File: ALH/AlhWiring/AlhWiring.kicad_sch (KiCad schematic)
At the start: 18 parts, among them J317 Relay_109, SW1 SW_Push_Open, SW2 SW_Push, T10e_car Conn_01x10_Socket, T10e_engine Black Connector, T10h_car Conn_01x10_Socket, T10h_engine Blue Connector, T10w_car Conn_01x10_Socket, T10w_engine White Connector, T14a_car 14pin Connector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

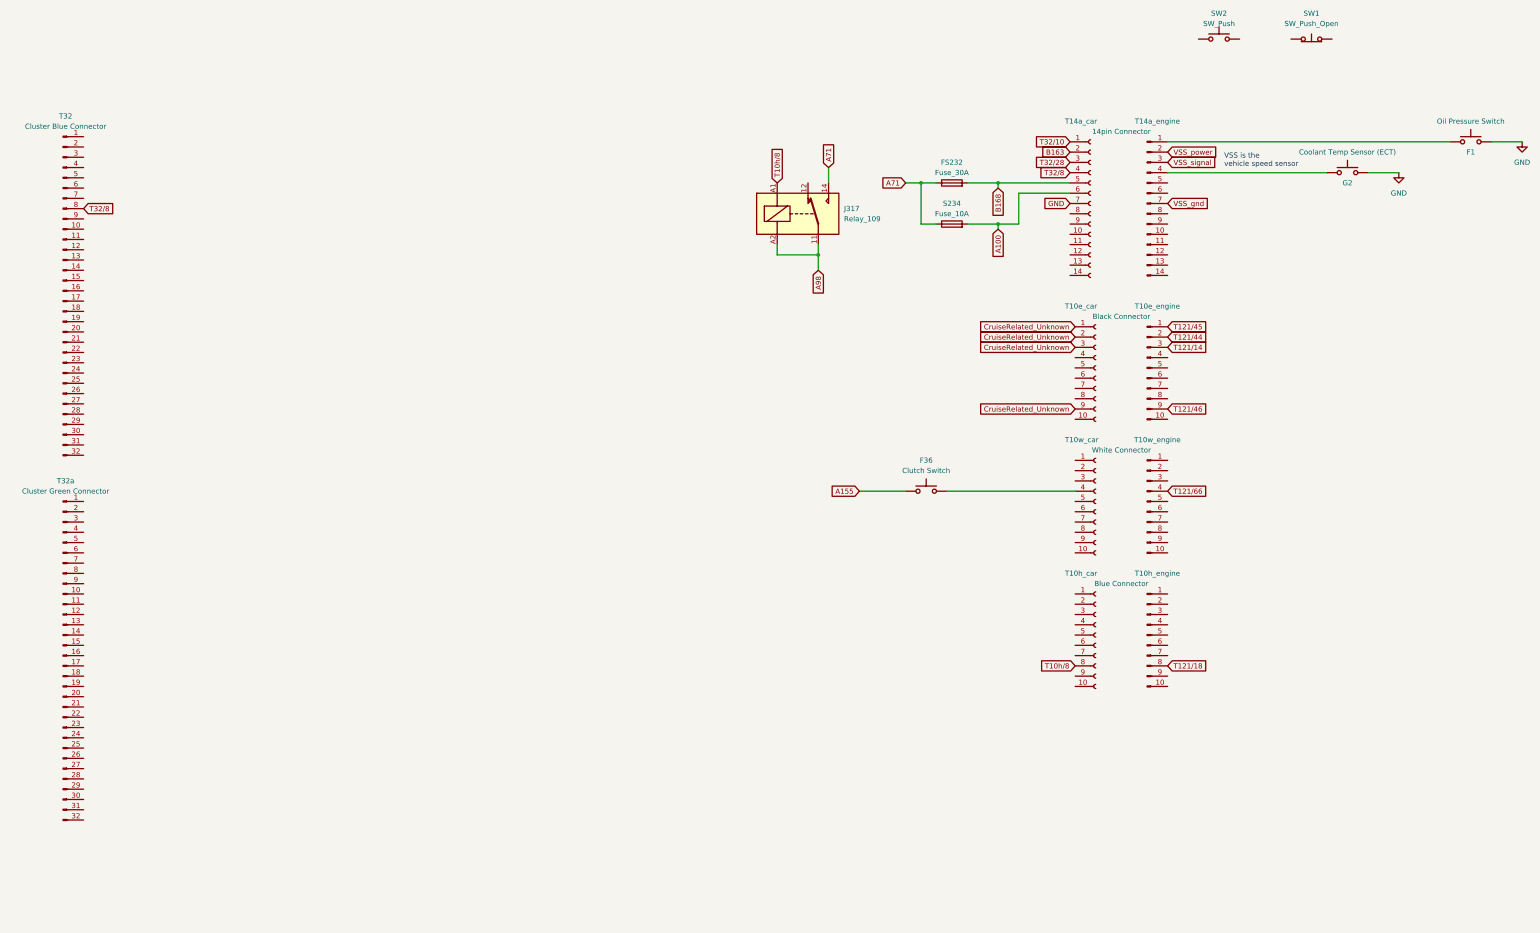
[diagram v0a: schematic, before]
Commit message: Finish ALH diagram.  Few parts still need to be reviewed.
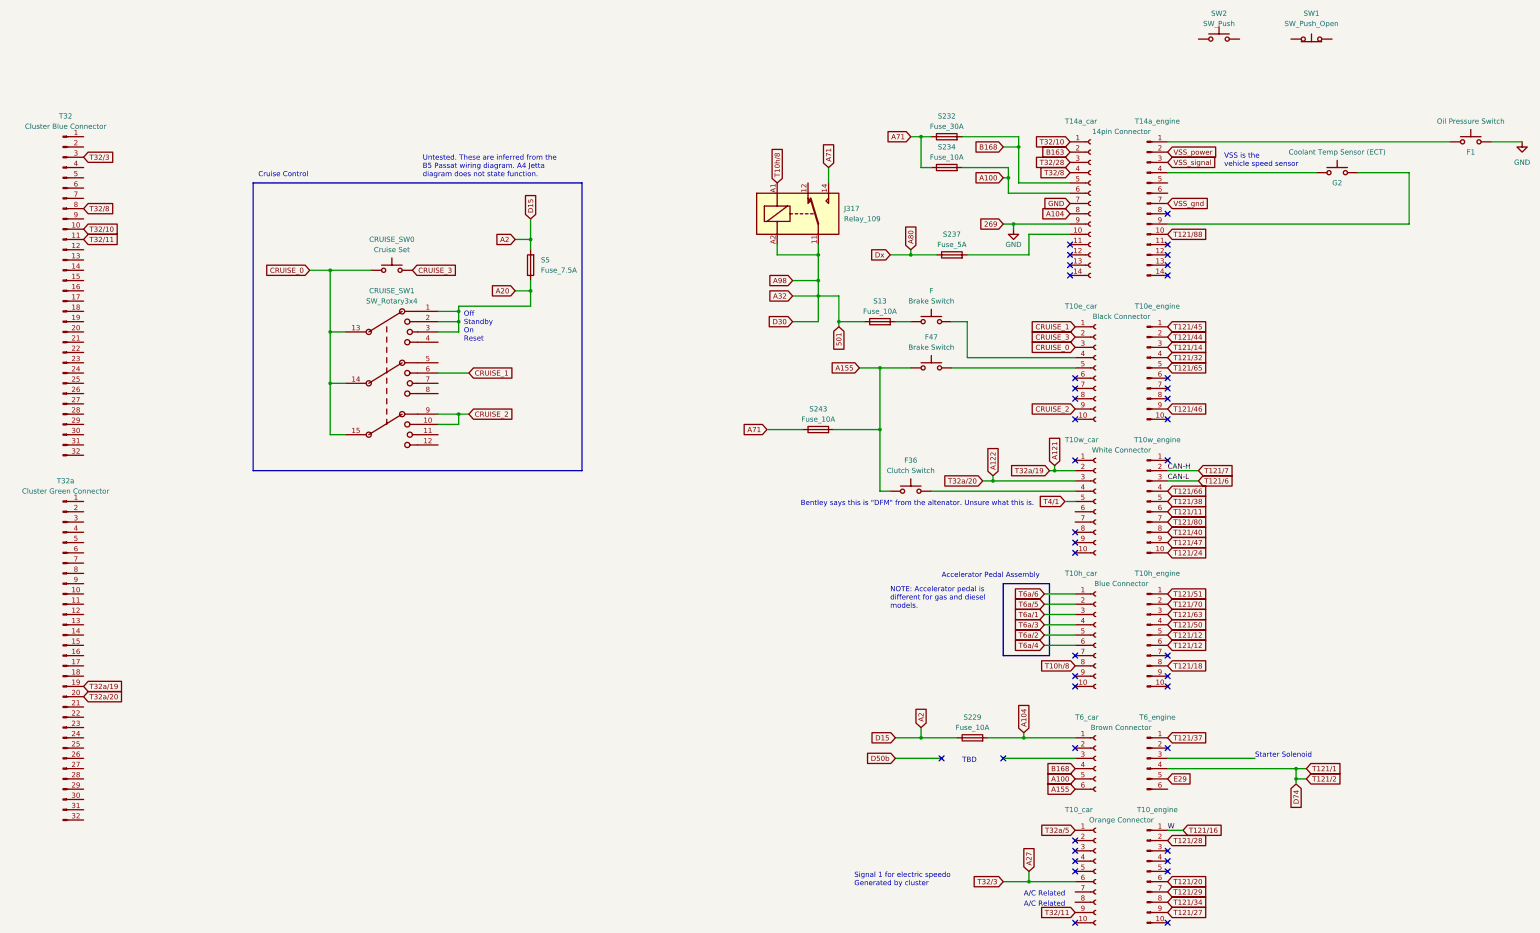
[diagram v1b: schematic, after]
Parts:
- added CRUISE_SW0: Cruise Set, symbol Switch:SW_Push
- added CRUISE_SW1: SW_Rotary3x4, symbol Switch:SW_Rotary3x4
- added F, F47: Brake Switch, symbol Switch:SW_Push
- added S13, S229, S243: Fuse_10A, symbol Device:Fuse
- added S237: Fuse_5A, symbol Device:Fuse
- added S5: Fuse_7.5A, symbol Device:Fuse
- added T10_car: Conn_01x10_Socket, symbol Connector:Conn_01x10_Socket
- added T10_engine: Orange Connector, symbol Connector:Conn_01x10_Pin
- added T6_car: Brown Connector, symbol Connector:Conn_01x06_Socket
- added T6_engine: Conn_01x06_Pin, symbol Connector:Conn_01x06_Pin
- renumbered FS232 to S232
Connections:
- net A100: now also T6_car.5 (Pin_5)
- net A155: now also F47.1, S243.2, T6_car.6 (Pin_6)
- net A71: now also S243.1
- net B168: now also T6_car.4 (Pin_4)
- net GND: now also T14a_car.9 (Pin_9); no longer G2.2
- net T32/10: now also T32.10 (Pin_10)
- net T32/11: now reaches T32.11 (Pin_11)
- net T32/11: now also T10_car.9 (Pin_9)
- net A27: now reaches T32.3 (Pin_3)
- net A27: now also T10_car.6 (Pin_6)
- net T121/24: now reaches T10w_engine.10 (Pin_10)
- net T121/7: now reaches T10w_engine.2 (Pin_2)
- net T121/6: now reaches T10w_engine.3 (Pin_3)
- net T121/38: now reaches T10w_engine.5 (Pin_5)
- net T121/11: now reaches T10w_engine.6 (Pin_6)
- net T121/80: now reaches T10w_engine.7 (Pin_7)
- net T121/40: now reaches T10w_engine.8 (Pin_8)
- net T121/47: now reaches T10w_engine.9 (Pin_9)
- net T121/32: now reaches T10e_engine.4 (Pin_4)
- net T121/65: now reaches T10e_engine.5 (Pin_5)
- net T121/51: now reaches T10h_engine.1 (Pin_1)
- net T121/70: now reaches T10h_engine.2 (Pin_2)
- net T121/63: now reaches T10h_engine.3 (Pin_3)
- net T121/50: now reaches T10h_engine.4 (Pin_4)
- net T121/12: now reaches T10h_engine.5 (Pin_5)
- net T121/12: now also T10h_engine.6 (Pin_6)
- net A121: now reaches T10w_car.2 (Pin_2)
- net A121: now also T32a.19 (Pin_19)
- net A122: now reaches T10w_car.3 (Pin_3)
- net A122: now also T32a.20 (Pin_20)
- net T4/1: now reaches T10w_car.5 (Pin_5)
- net at T14a_car.10 (Pin_10): now also S237.2
- net A104: now reaches T14a_car.8 (Pin_8)
- net A104: now also S229.2, T6_car.1 (Pin_1)
- net T121/88: now reaches T14a_engine.10 (Pin_10)
- net at T14a_engine.9 (Pin_9): now also G2.2
- net T6a/6: now reaches T10h_car.1 (Pin_1)
- net T6a/5: now reaches T10h_car.2 (Pin_2)
- net T6a/1: now reaches T10h_car.3 (Pin_3)
- net T6a/3: now reaches T10h_car.4 (Pin_4)
- net T6a/2: now reaches T10h_car.5 (Pin_5)
- net T6a/4: now reaches T10h_car.6 (Pin_6)
- net at T10e_car.4 (Pin_4): now also F.2
- net at T10e_car.5 (Pin_5): now also F47.2
- net A98 renamed 501
- net 501: now also S13.1
- removed net CruiseRelated_Unknown: T10e_car.1 (Pin_1), T10e_car.2 (Pin_2), T10e_car.3 (Pin_3), T10e_car.9 (Pin_9)
- new net: F.1, S13.2
- new net A2: S229.1, S5.2
- new net A20: CRUISE_SW1.1, CRUISE_SW1.2, CRUISE_SW1.3, S5.1
- new net A80: S237.1
- new net CRUISE_0: CRUISE_SW0.1, CRUISE_SW1.13, CRUISE_SW1.14, CRUISE_SW1.15, T10e_car.3 (Pin_3)
- new net CRUISE_1: CRUISE_SW1.6, T10e_car.1 (Pin_1)
- new net CRUISE_2: CRUISE_SW1.10, CRUISE_SW1.9, T10e_car.9 (Pin_9)
- new net CRUISE_3: CRUISE_SW0.2, T10e_car.2 (Pin_2)
- new net D74: T6_engine.4 (Pin_4)
- new net E29: T6_engine.5 (Pin_5)
- new net T121/16: T10_engine.1 (Pin_1)
- new net T121/20: T10_engine.6 (Pin_6)
- new net T121/27: T10_engine.9 (Pin_9)
- new net T121/28: T10_engine.2 (Pin_2)
- new net T121/29: T10_engine.7 (Pin_7)
- new net T121/34: T10_engine.8 (Pin_8)
- new net T121/37: T6_engine.1 (Pin_1)
- new net T32a/5: T10_car.1 (Pin_1)
- no-connect marks 0 -> 41
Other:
- note added: "A/C Related"
- note added: "Accelerator Pedal Assembly"
- note added: "Bentley says this is "DFM" from the altenator. Unsure what this is."
- note added: "Cruise Control"
- note added: "NOTE: Accelerator pedal is different for gas and diesel models."
- note added: "Off Standby On Reset"
- note added: "Signal 1 for electric speedo Generated by cluster"
- note added: "Starter Solenoid"
- note added: "TBD"
- note added: "Untested. These are inferred from the B5 Passat wiring diagram. A4 Jetta diagram does not state function."
- moved on the sheet: F36, G2, S232, S234
